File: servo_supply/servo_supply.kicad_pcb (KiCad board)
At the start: 2 copper layers, 46.3 x 37.8 mm, 26 parts, among them J1 Conn_01x02_Pin, J2 Conn_01x02_Pin, J3 Conn_01x02_Pin, U1 AZ1117-ADJ, U2 AZ1117-ADJ, U3 AZ1117-ADJ

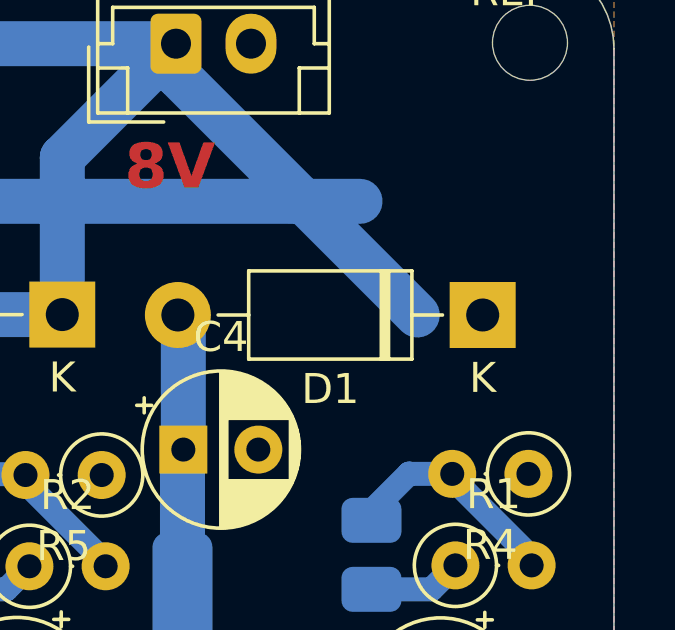
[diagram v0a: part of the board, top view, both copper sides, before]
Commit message: feat:接続ミスを修正
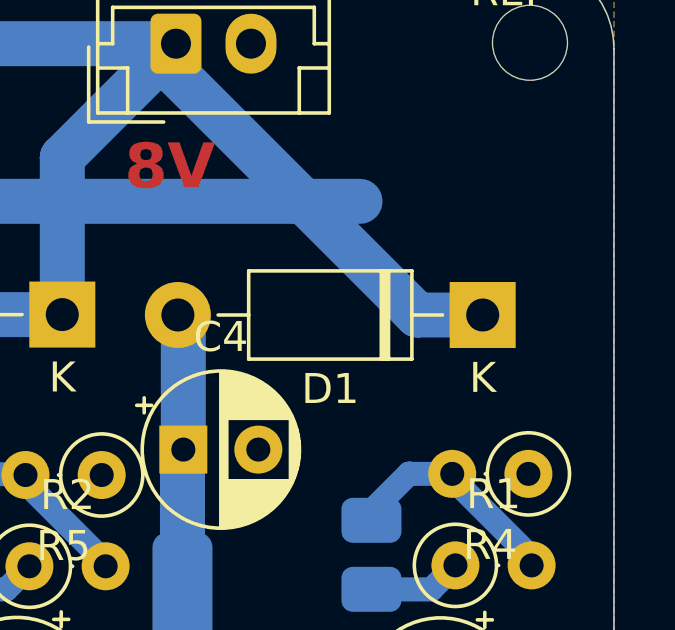
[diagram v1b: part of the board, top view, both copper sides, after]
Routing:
- net +8V: track 89.1 -> 91.3 mm
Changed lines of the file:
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@@
+	)
+	(segment
+		(start 169.1 76.03)
+		(end 177.144 84.074)
+		(width 1.5)
+		(layer "B.Cu")
+		(net 9)
 	)
 	(segment
 		(start 151.3 76.86)
 		(end 152.98 75.18)
+		(width 1.5)
+		(layer "B.Cu")
+		(net 9)
+	)
+	(segment
+		(start 169.1 75.03)
+		(end 169.1 76.03)
 		(width 1.5)
 		(layer "B.Cu")
@@
 	)
 	(segment
-		(start 169.1 75.03)
-		(end 169.1 76.03)
+		(start 151.3 84.08)
+		(end 151.3 76.86)
 		(width 1.5)
 		(layer "B.Cu")
@@
 	)
 	(segment
-		(start 169.1 76.03)
-		(end 177.144 84.074)
+		(start 177.144 84.074)
+		(end 179.324 84.074)
 		(width 1.5)
 		(layer "B.Cu")
-		(net 9)
-	)
-	(segment
-		(start 151.3 84.08)
-		(end 151.3 76.86)
-		(width 1.5)
-		(layer "B.Cu")

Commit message: feat:bug修正
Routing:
- net +8V: track 91.3 -> 90.7 mm
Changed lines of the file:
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@@
 	)
 	(segment
-		(start 175.235 80.285)
+		(start 174.295 81.225)
+		(end 173.355 80.285)
+		(width 1.5)
+		(layer "B.Cu")
+		(net 9)
+	)
+	(segment
+		(start 173.355 80.285)
 		(end 157.085 80.285)
 		(width 1.5)
